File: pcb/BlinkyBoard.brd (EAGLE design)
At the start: 25.2 x 10 mm, 25 parts, among them Q1 16 MHz

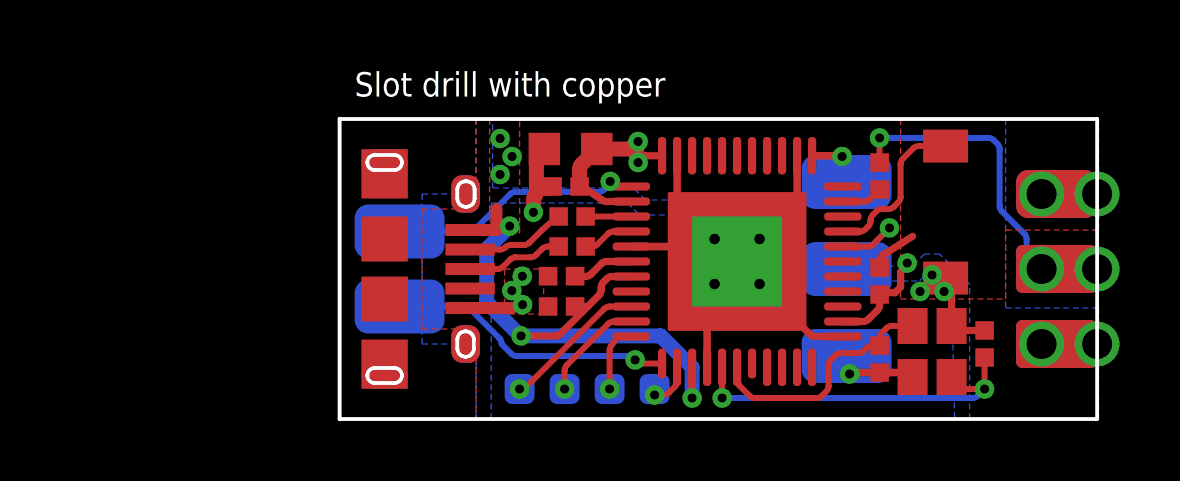
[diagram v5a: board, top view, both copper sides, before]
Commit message: Remove some excess noise on the silk
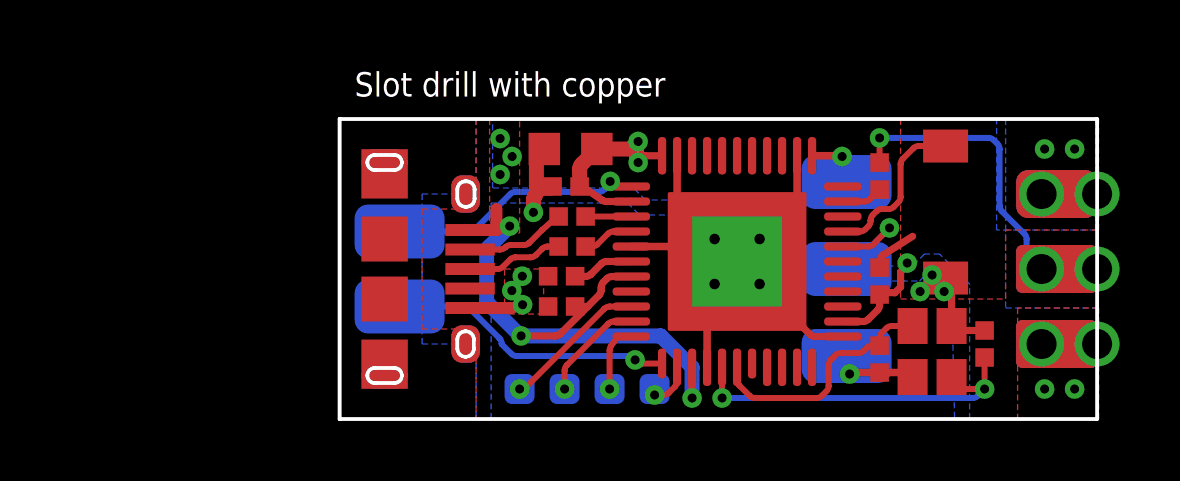
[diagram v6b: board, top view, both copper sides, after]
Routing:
- net VCC: vias 10 -> 12
- net GND: vias 8 -> 10
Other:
- board text removed: "/Users/matt/Blinkinlabs-Projects/BlinkyTape/pcb/Untitled.BMP"

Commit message: Fix output resistor value
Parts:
- R3: value ?? -> 200
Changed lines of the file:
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@@
 <?xml version="1.0" encoding="utf-8"?>
 <!DOCTYPE eagle SYSTEM "eagle.dtd">
-<eagle version="7.2.0">
+<eagle version="7.5.0">
 <drawing>
 <settings>
@@
 <element name="U$15" library="blinkiverse" package="OSHW-LOGO-S" value="" x="13.29" y="8.1" rot="MR0"/>
 <element name="U$9" library="blinkiverse" package="WS2812B_CONNECTOR" value="WS2812B_CONNECTOR" x="23.9" y="5" rot="MR180"/>
-<element name="R3" library="blinkiverse" package="RES_0402_KEMET_MEDIAN" value="??" x="18" y="8.1" rot="R90"/>
+<element name="R3" library="blinkiverse" package="RES_0402_KEMET_MEDIAN" value="200" x="18" y="8.1" rot="R90"/>
 <element name="U$7" library="blinkinlabs" package="BUTTON_2P_SMD" value="" x="20.2" y="6.9" smashed="yes" rot="R270">
 <attribute name="VALUE" x="17.2" y="9.9" size="1.27" layer="27" rot="R270"/>

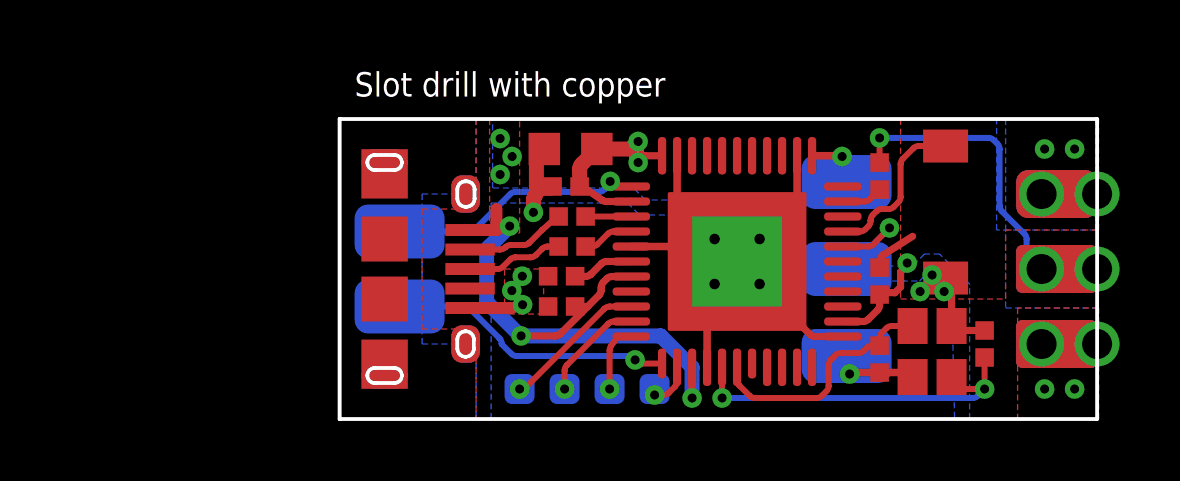
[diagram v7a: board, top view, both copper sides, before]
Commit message: Add ESD components, needs routing
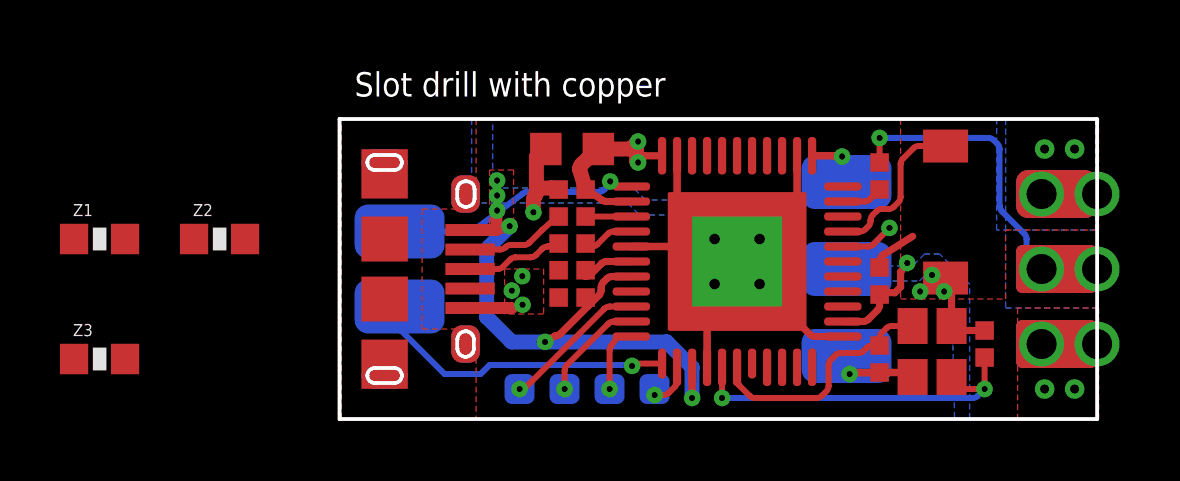
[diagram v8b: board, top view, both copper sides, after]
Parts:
- added Z1, Z2, Z3: PGB1010603, PaxInstrument-T400:SPARKFUN-RESISTORS_0603-RES
- moved C3 0.46 mm to (7.75, 4.05)
- moved C5 0.40 mm to (7.75, 4.96)
- moved C2 0.22 mm to (7.75, 7.65)
- moved R1 0.10 mm to (7.75, 5.85)
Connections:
- net N$2 renamed UCAP
- net N$8 renamed XTAL2
- net N$9 renamed XTAL1
- removed net SHIELD: U$4.PAD$1, U$4.PAD$10, U$4.PAD$2, U$4.PAD$3, U$4.PAD$4, U$4.PAD$5, U$4.PAD$6, U$4.PAD$7, U$4.PAD$8, U$4.PAD$9
- net D+_IN: now also Z1.2
- net D-_IN: now also Z2.2
- net GND: now also U$4.PAD$1, U$4.PAD$10, U$4.PAD$2, U$4.PAD$3, U$4.PAD$4, U$4.PAD$5, U$4.PAD$6, U$4.PAD$7, U$4.PAD$8, U$4.PAD$9, Z1.1, Z2.1, Z3.1
- net VCC: now also Z3.2
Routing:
- net D11: track 9.52 -> 10.3 mm
- net VCC: track 30.5 -> 29.9 mm
- removed copper zone on layer 1, net SHIELD
- removed copper zone on layer 16, net SHIELD
